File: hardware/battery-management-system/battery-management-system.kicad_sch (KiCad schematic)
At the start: 4 parts

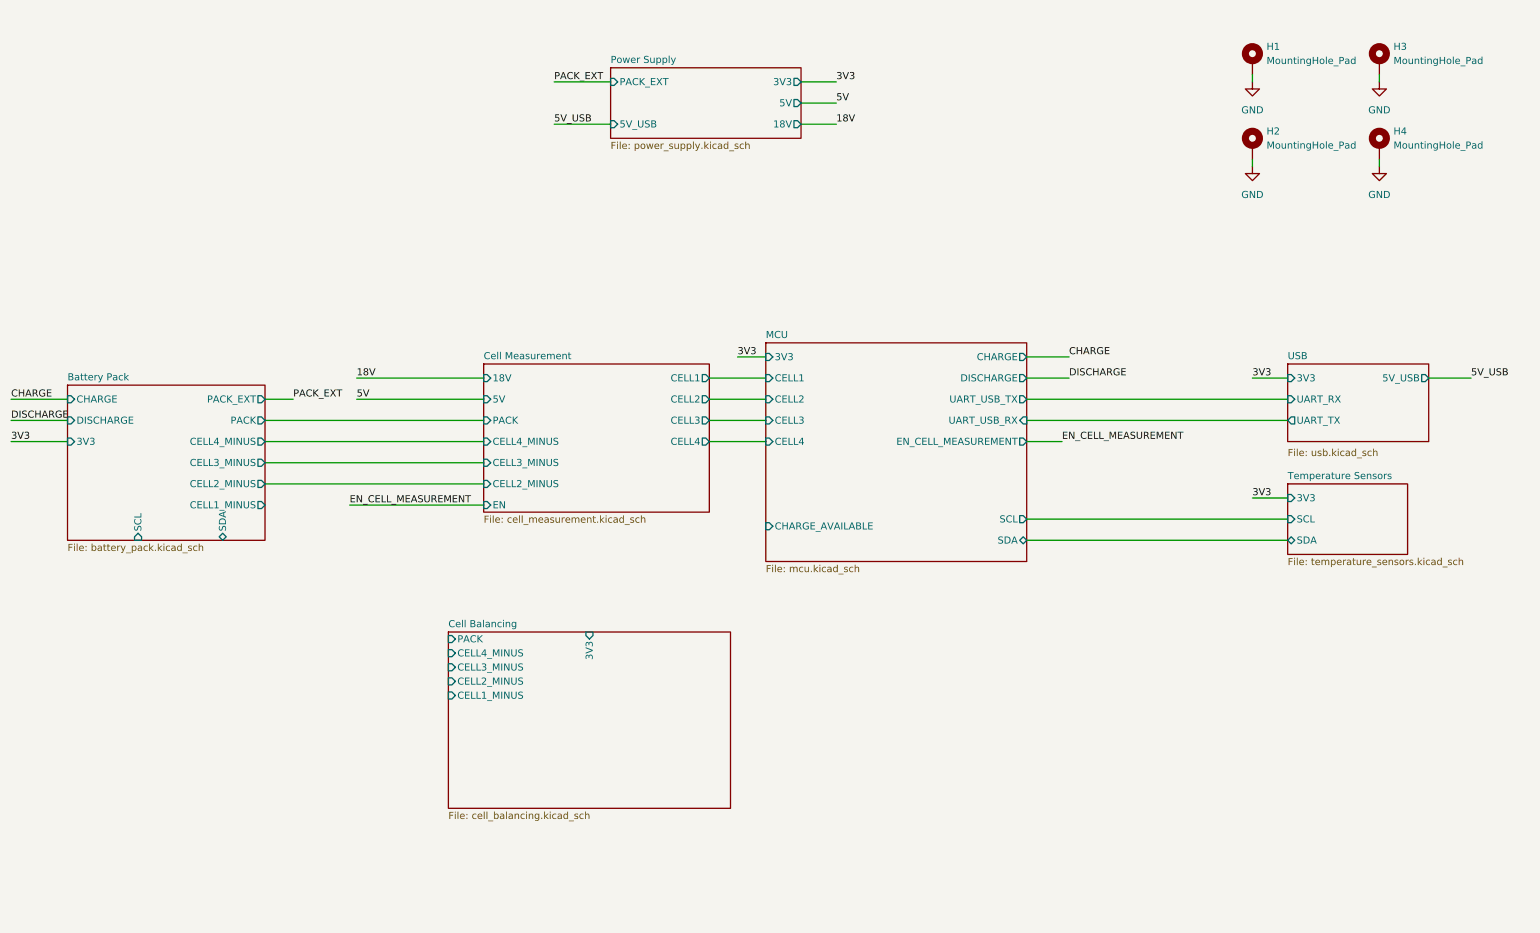
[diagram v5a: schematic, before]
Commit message: finish cell balancing schematic
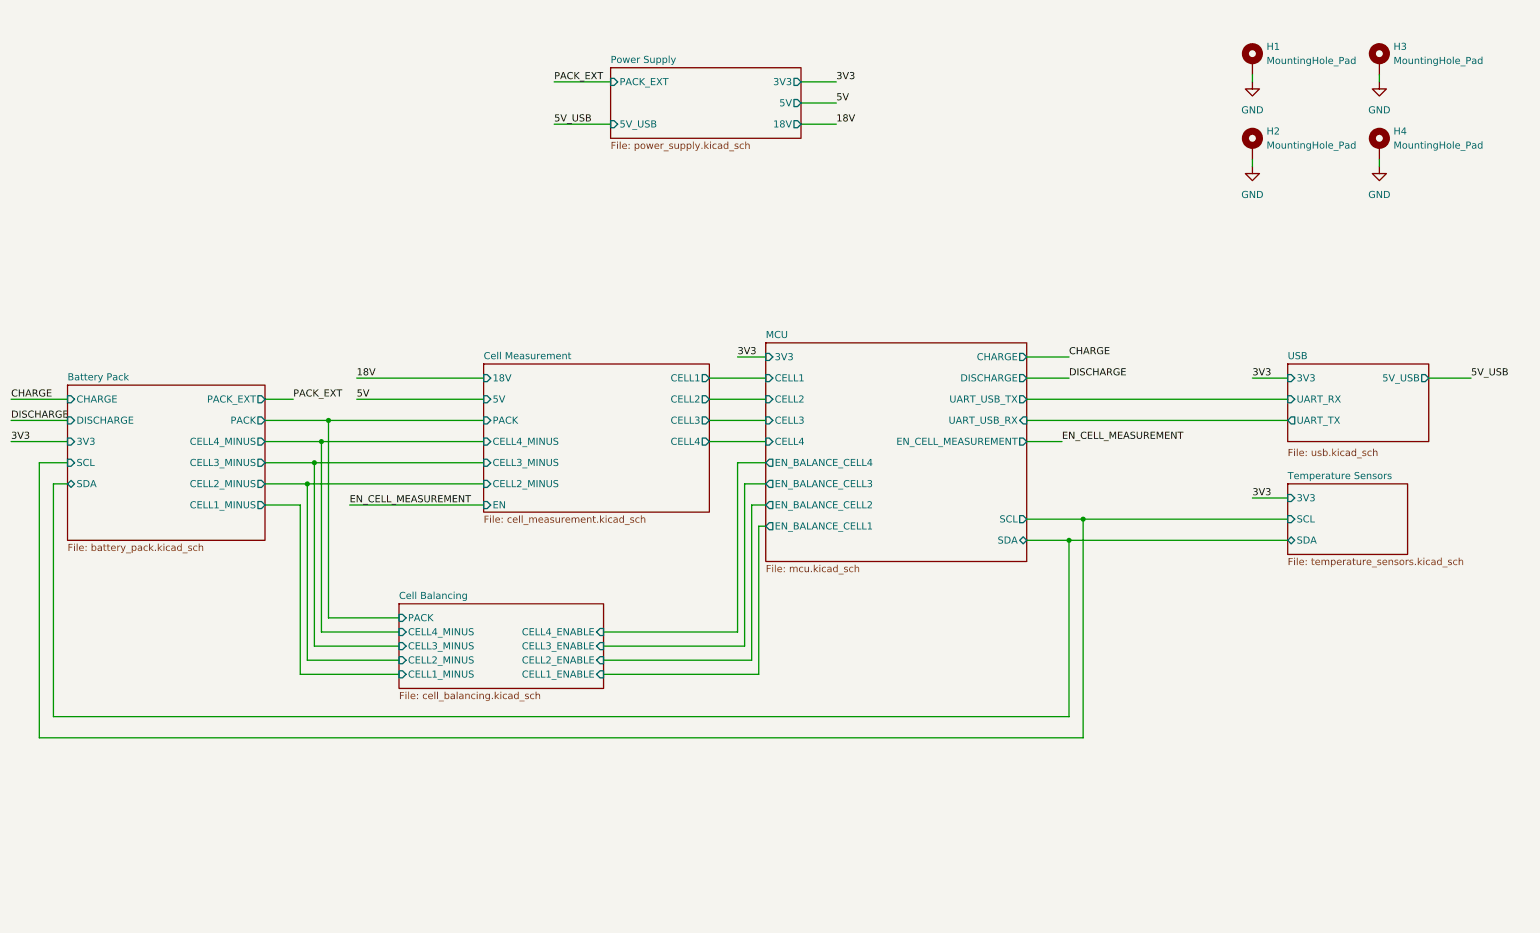
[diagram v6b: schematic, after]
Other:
- sheet Cell Balancing ports: added CELL1_ENABLE, CELL2_ENABLE, CELL3_ENABLE, CELL4_ENABLE; removed 3V3
- sheet MCU ports: added EN_BALANCE_CELL1, EN_BALANCE_CELL2, EN_BALANCE_CELL3, EN_BALANCE_CELL4; removed CHARGE_AVAILABLE

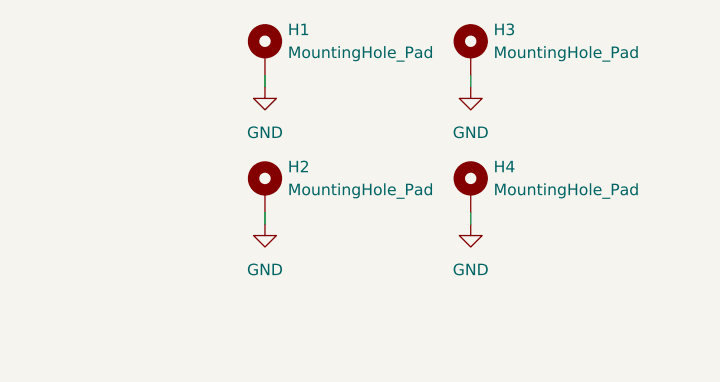
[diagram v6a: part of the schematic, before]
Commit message: add snubber circuit
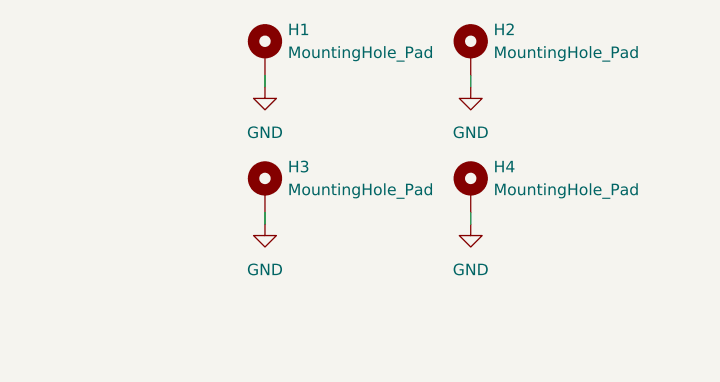
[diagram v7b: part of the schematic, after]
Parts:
- renumbered H3 to H2, H2 to H3
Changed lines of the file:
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@@
 		(dnp no)
 		(fields_autoplaced yes)
-		(property "Reference" "H3"
+		(property "Reference" "H2"
 			(at 261.62 20.32 0)
 			(effects
@@
 			(project "battery-management-system"
 				(path "/5272f0ff-3069-41a9-bca2-80beede8b4b2"
-					(reference "H3")
+					(reference "H2")
 					(unit 1)
 				)
@@
 		(dnp no)
 		(fields_autoplaced yes)
-		(property "Reference" "#PWR02"
+		(property "Reference" "#PWR03"
 			(at 236.22 48.26 0)
 			(effects
@@
 			(project "battery-management-system"
 				(path "/5272f0ff-3069-41a9-bca2-80beede8b4b2"
-					(reference "#PWR02")
+					(reference "#PWR03")
 					(unit 1)
 				)
@@
 		(dnp no)
 		(fields_autoplaced yes)
-		(property "Reference" "H2"
+		(property "Reference" "H3"
 			(at 238.76 35.56 0)
 			(effects
@@
 			(project "battery-management-system"
 				(path "/5272f0ff-3069-41a9-bca2-80beede8b4b2"
-					(reference "H2")
+					(reference "H3")
 					(unit 1)
 				)
@@
 		(dnp no)
 		(fields_autoplaced yes)
-		(property "Reference" "#PWR03"
+		(property "Reference" "#PWR02"
 			(at 259.08 33.02 0)
 			(effects
@@
 			(project "battery-management-system"
 				(path "/5272f0ff-3069-41a9-bca2-80beede8b4b2"
-					(reference "#PWR03")
-					(unit 1)
-				)
+					(reference "#PWR02")
+					(unit 1)
+				)
